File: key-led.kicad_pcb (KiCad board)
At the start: 2 copper layers, 30.5 x 24.1 mm, 8 parts, among them J1 Conn_01x01_Female, J2 Conn_01x01_Female, J3 Conn_01x01_Female, J4 Conn_01x01_Female, J5 Conn_01x01_Female, J6 Conn_01x01_Female, SW1 SW_Push_45deg

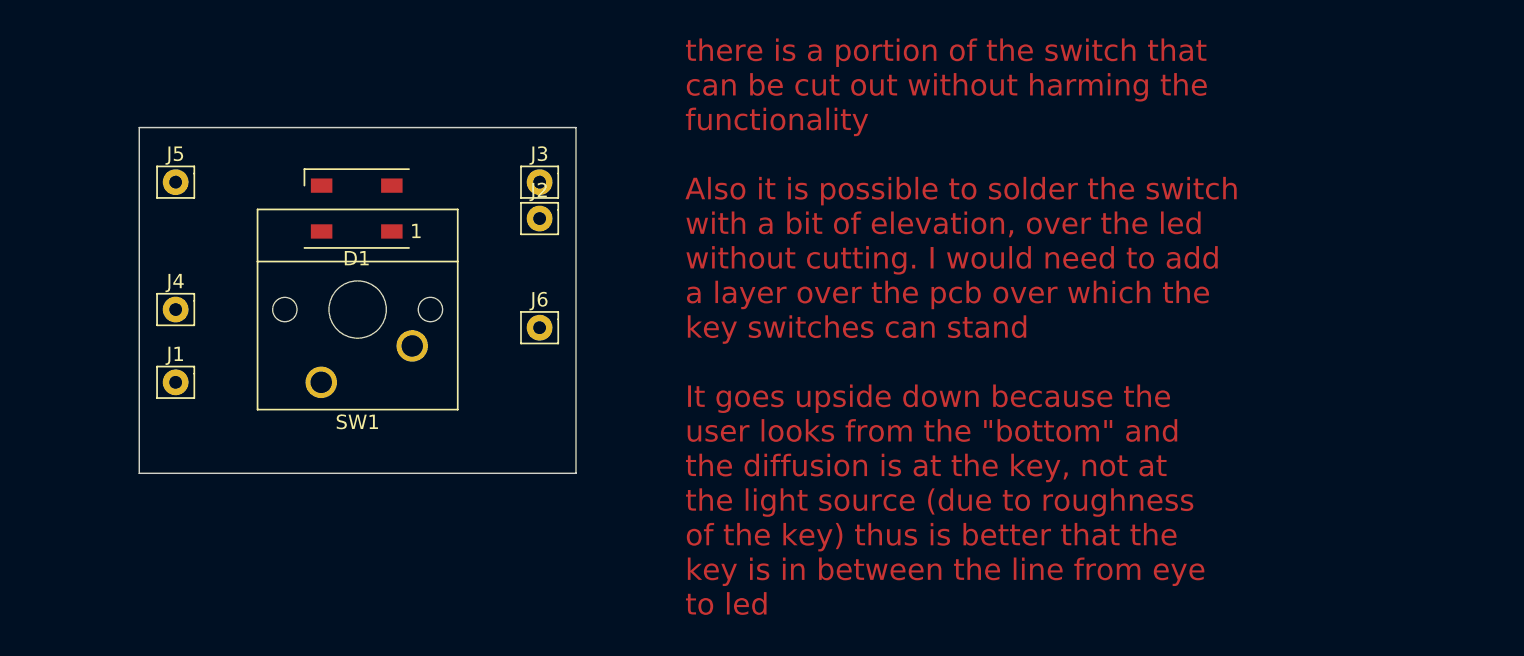
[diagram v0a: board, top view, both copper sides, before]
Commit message: 4x row design, layout and route
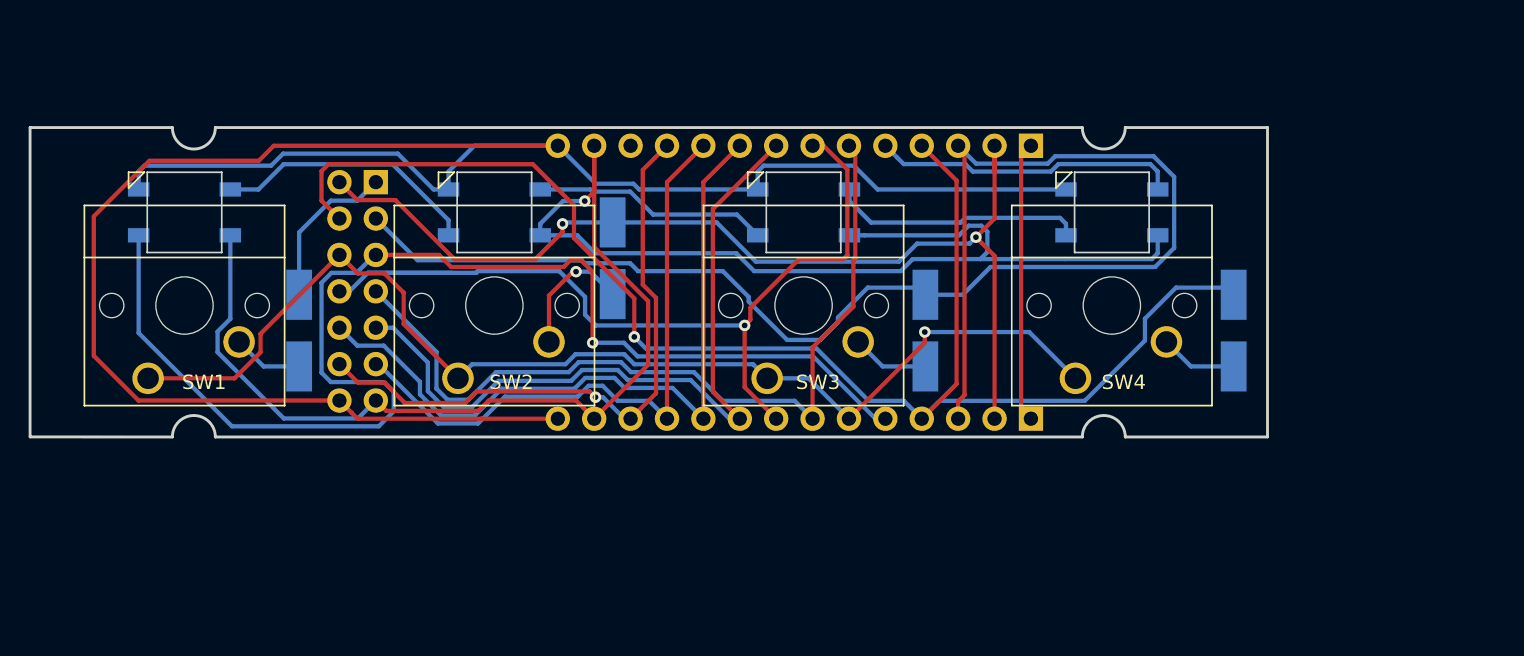
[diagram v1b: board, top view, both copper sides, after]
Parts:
- removed J1, J2, J3, J4, J5, J6: Conn_01x01_Female, Connector_Pin:Pin_D0.9mm_L10.0mm_W2.4mm_FlatFork
- added D2: WS2812B, key-led:LED_WS2812B_PLCC4-back-mount, B.Cu at (111.1, 138.0)
- added D3: WS2812B, key-led:LED_WS2812B_PLCC4-back-mount, B.Cu at (132.7, 138.0)
- added D4: WS2812B, key-led:LED_WS2812B_PLCC4-back-mount, B.Cu at (154.2, 138.0)
- added D5: FM4004-W, Diode_SMD:D_SMA_Handsoldering, B.Cu at (97.5, 146.2)
- added D6: FM4004-W, Diode_SMD:D_SMA_Handsoldering, B.Cu at (119.4, 141.2)
- added D7: FM4004-W, Diode_SMD:D_SMA_Handsoldering, B.Cu at (141.2, 146.2)
- added D8: FM4004-W, Diode_SMD:D_SMA_Handsoldering, B.Cu at (162.7, 146.2)
- added J-INS1: Conn_02x07_Odd_Even, Connector_PinHeader_2.54mm:PinHeader_2x07_P2.54mm_Vertical, B.Cu at (102.9, 135.9)
- added J-ins2: Conn_01x14_Male, Connector_PinHeader_2.54mm:PinHeader_1x14_P2.54mm_Vertical, B.Cu at (148.6, 152.4)
- added J-outs2: Conn_01x14_Female, Connector_PinHeader_2.54mm:PinHeader_1x14_P2.54mm_Vertical, B.Cu at (148.6, 133.3)
- added SW2: SW_Push_45deg, key-led:SW_Cherry_MX_1.00u_PCB, F.Cu at (108.6, 149.6)
- added SW3: SW_Push_45deg, key-led:SW_Cherry_MX_1.00u_PCB, F.Cu at (130.2, 149.6)
- added SW4: SW_Push_45deg, key-led:SW_Cherry_MX_1.00u_PCB, F.Cu at (151.7, 149.6)
- D1: footprint LED_SMD:LED_WS2812B_PLCC4_5.0x5.0mm_P3.2mm -> key-led:LED_WS2812B_PLCC4-back-mount; moved to B.Cu
- moved SW1 12.1 mm to (87.0, 149.6)
- moved D1 12.0 mm to (89.5, 138.0), turned to 0 degrees
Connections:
- D1 pad 1: Net-(D1-Pad1) -> VCC
- D1 pad 3: Net-(D1-Pad3) -> GND
- D1 pad 4: Net-(D1-Pad4) -> /LED-DIN-1
- SW1 pad 1: Net-(J1-Pad1) -> /BUTTON-ROW
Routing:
- net GND: track 0.00 -> 151.3 mm
- net VCC: track 0.00 -> 127.3 mm, vias 0 -> 1
- net /BUTTON-COL-3: track 0.00 -> 104.9 mm
- net /BUTTON-COL-4: track 0.00 -> 103.9 mm, vias 0 -> 1
- net /LED-DIN-1: track 0.00 -> 89.2 mm, vias 0 -> 1
- net /BUTTON-ROW: track 0.00 -> 80.7 mm, vias 0 -> 1
- net /BUTTON-COL-2: track 0.00 -> 71.8 mm, vias 0 -> 2
- net /ROW-UP-IN2: track 0.00 -> 63.2 mm, vias 0 -> 1
- net /ROW-UP-IN1: track 0.00 -> 58.3 mm
- net /ROW-UP-IN3: track 0.00 -> 53.0 mm
- net /ROW-UP-IN4: track 0.00 -> 50.8 mm
- net /ROW-UP-IN5: track 0.00 -> 44.2 mm
- net /ROW-UP-IN6: track 0.00 -> 44.1 mm, vias 0 -> 1
- net /BUTTON-COL-1: track 0.00 -> 30.8 mm
- net /LED-DOUT-1: track 0.00 -> 21.4 mm
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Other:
- board size 30.5 x 24.1 mm -> 86.4 x 21.6 mm
- net class Default: clearance 0.2 -> 0.25; trace_width 0.25 -> 0.3
- rule trace_clearance: 0.2 -> 0.25

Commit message: improve position
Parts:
- moved D8 16.8 mm to (145.9, 146.2)
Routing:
- net /BUTTON-COL-3: track 104.9 -> 69.9 mm, vias 0 -> 1
- net /BUTTON-COL-4: track 103.9 -> 89.2 mm
- net Net-(D8-Pad2): track 5.40 -> 14.8 mm
- net VCC: track 127.3 -> 129.0 mm

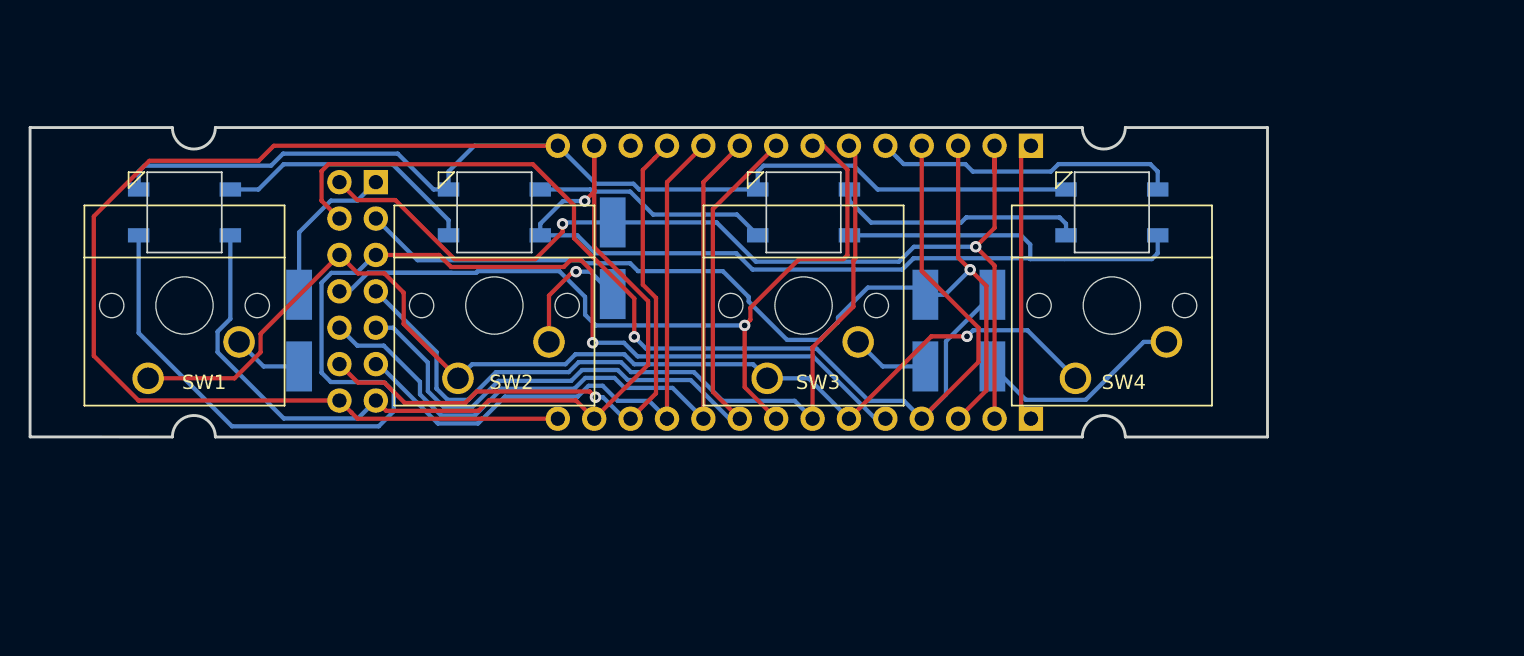
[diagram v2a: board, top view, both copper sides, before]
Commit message: shaped routes in angles, like in the old pcbs
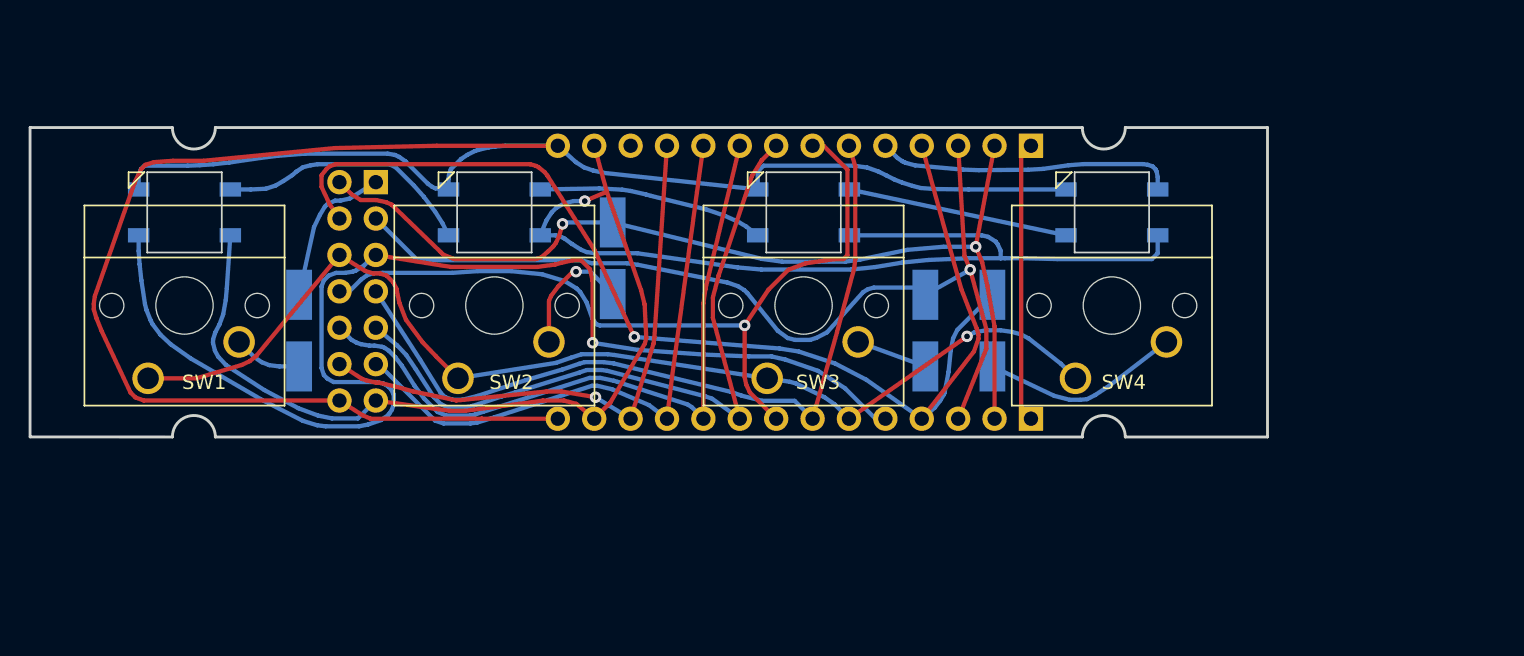
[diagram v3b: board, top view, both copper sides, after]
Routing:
- net VCC: track 129.0 -> 120.5 mm
- net /ROW-UP-IN2: track 63.2 -> 56.2 mm
- net /BUTTON-COL-4: track 89.2 -> 85.3 mm
- net /BUTTON-COL-2: track 71.5 -> 67.6 mm
- net /LED-DIN-1: track 89.2 -> 85.3 mm
- net GND: track 151.3 -> 147.5 mm
- net /ROW-UP-IN3: track 53.0 -> 49.4 mm
- net /BUTTON-ROW: track 80.4 -> 76.8 mm
- net /ROW-UP-IN1: track 58.3 -> 55.3 mm
- net /ROW-UP-IN6: track 44.1 -> 41.3 mm
- net /ROW-UP-IN4: track 50.8 -> 48.5 mm
- net Net-(D3-Pad2): track 17.7 -> 15.5 mm
- net /BUTTON-COL-3: track 69.9 -> 67.7 mm
- net /ROW-UP-IN5: track 44.2 -> 42.2 mm
- net Net-(D8-Pad2): track 14.8 -> 13.9 mm
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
